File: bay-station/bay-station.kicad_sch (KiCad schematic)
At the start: 0 parts

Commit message: Add Power/BMS sheets: reverse-polarity protection, TVS, decoupling
Wristband power_bms.kicad_sch:
- JST-PH battery in -> AO3401A P-MOSFET reverse-polarity 'ideal diode'
  (source=batt+, gate pulled to GND via 100k) -> ESD5B5.0ST1G TVS across
  VBAT-GND -> DW01A+FS8205A single-cell protection (wired per Fortune
  Semiconductor's real datasheet application circuit) -> MCP73831 charger
  (USB-C power-only in, 6.8k PROG -> ~147mA, datasheet-exact CIN/COUT)
- NINA-B111/DWM3000 deliberately deferred to a future radio_mcu sheet
  (this sheet just produces a decoupled VBAT rail) -- see
  wristband/power_bms_notes.md
- ERC: 0 errors, 1 cosmetic warning (documented below)

Bay-station power_bms.kicad_sch:
- Barrel jack + USB-C power-only input (shared +5V_IN, each with reverse-
  polarity/TVS protection) alongside a backup Li-Ion input protected by
  its own AO3401A ideal-diode + TVS
- MCP73871 charge/power-path IC per Microchip's real typical application
  circuit (power-path/AC-DC-adapter mode, PROG1/PROG3 sized for 500mA
  fast-charge / 50mA termination, VPCC divider from the datasheet's own
  worked example) -> MAX17048 fuel gauge
- ESP32-S3-WROOM-1/DWM3000 anchors deferred to future connectivity/
  uwb_anchors sheets -- this sheet produces +VSYS (unregulated, tracks
  battery/input -- a dedicated 3.3V reg stage is a real open item) and
  VBATT_PROT
- ERC: 8 violations (1 error, 7 warnings), all single-member nets/pins
  reserved for hardware that doesn't exist until the connectivity sheet
  is built (e.g. MAX17048's SCL has no I2C host placed yet) -- see
  bay-station/power_bms_notes.md

Both sheets use global labels for net identity (no drawn wires), matching
the sibling wristband-alarm project's convention, and only reference
already-imported library parts plus KiCad-default generics (P-MOSFET,
TVS, R/C) -- no new custom symbols were needed on either board.

Notable gotcha found and documented: kicad-cli silently fails to load
(and silently treats as EMPTY, no error) a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
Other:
- added sheet Power BMS (power_bms.kicad_sch)
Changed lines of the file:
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@@
 		(comment 1 "UWB rescue locator -- bay station: 4x UWB anchor array + connectivity MCU + longevity-focused BMS")
+	)
+	(sheet
+		(at 30 30)
+		(size 60 40)
+		(fields_autoplaced yes)
+		(stroke
+			(width 0.1524)
+			(type solid)
+		)
+		(fill
+			(color 0 0 0 0.0000)
+		)
+		(property "Sheetname" "Power BMS"
+			(at 30 28.5 0)
+			(effects
+				(font
+					(size 1.27 1.27)
+				)
+				(justify left bottom)
+			)
+		)
+		(property "Sheetfile" "power_bms.kicad_sch"
+			(at 30 71.5 0)
+			(effects
+				(font
+					(size 1.27 1.27)
+				)
+				(justify left top)
+			)
+		)
+		(instances
+			(project "bay-station"
+				(path "/543ba435-6cf4-448c-821e-3c5778b02e9c"
+					(page "2")
+				)
+			)
+		)
 	)
 	(sheet_instances

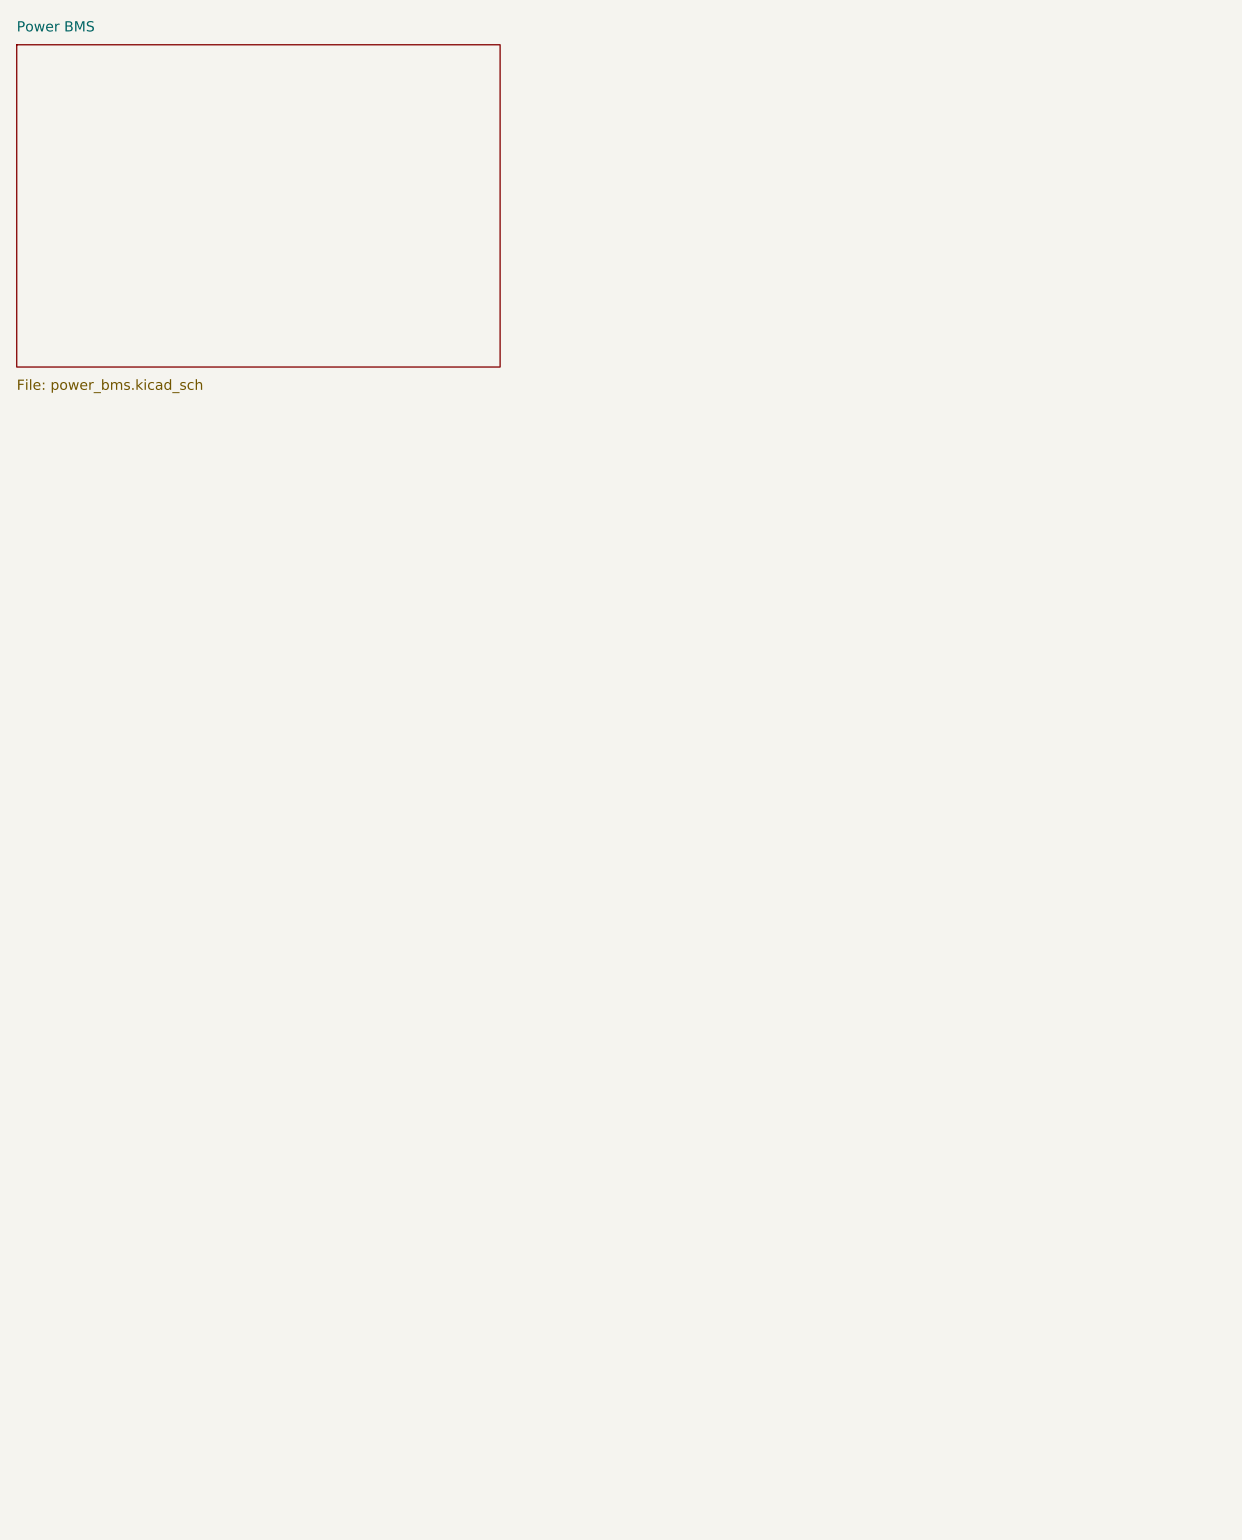
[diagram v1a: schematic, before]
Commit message: Add radio_mcu/mechanical (wristband) and connectivity/uwb_anchors/mechanical (bay-station) sheets
Placement-only pass, nothing wired (no wires, no global labels) -- per
request, this organizes the remaining confirmed components onto their
own hierarchical sheets rather than wiring them up yet:

Wristband:
- radio_mcu.kicad_sch: NINA-B111 (U3) + DWM3000 (U4), with 0603 decoupling
  caps placed near each supply pin (values are reasonable generic
  defaults, not yet confirmed against exact datasheet application-circuit
  numbers -- flagged in the sheet/README, revisit when wiring)
- mechanical.kicad_sch: 4x M2 mounting holes (H1-H4)

Bay-station:
- connectivity.kicad_sch: ESP32-S3-WROOM-1 (U3) + decoupling per
  Espressif's design guidelines (already cited in libs/README.md)
- uwb_anchors.kicad_sch: 4x DWM3000 anchor instances (U4-U7), each
  individually labeled and decoupled (values are typical-practice
  estimates, not independently re-verified against the datasheet's own
  application circuit -- flagged on the sheet itself)
- mechanical.kicad_sch: 4x mounting holes (H1-H4) + a note pointing at
  docs/decisions.md's open anchor-placement/enclosure item

Both boards: sheet hierarchy registered in the root .kicad_sch and the
project's sheets list, no reference-designator collisions with the
existing power_bms sheets. ERC shows the expected large jump in
'not connected'/'not driven' violations on the new sheets only (inherent
to placing components without wiring them) -- the existing power_bms
sheets' own violation counts are unchanged.

Also: bay-station's power_bms.kicad_sch/bay-station.kicad_sch/
bay-station.kicad_pro got silently reformatted to KiCad 10 file format by
a live KiCad GUI session that had the project open in the background
during this work (confirmed via reference-designator diff that no
component content was lost, just a version/format bump) -- wristband's
files are unaffected, still KiCad 8.0 format. Added bay-station's new
KiCad-10 '.history/' local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
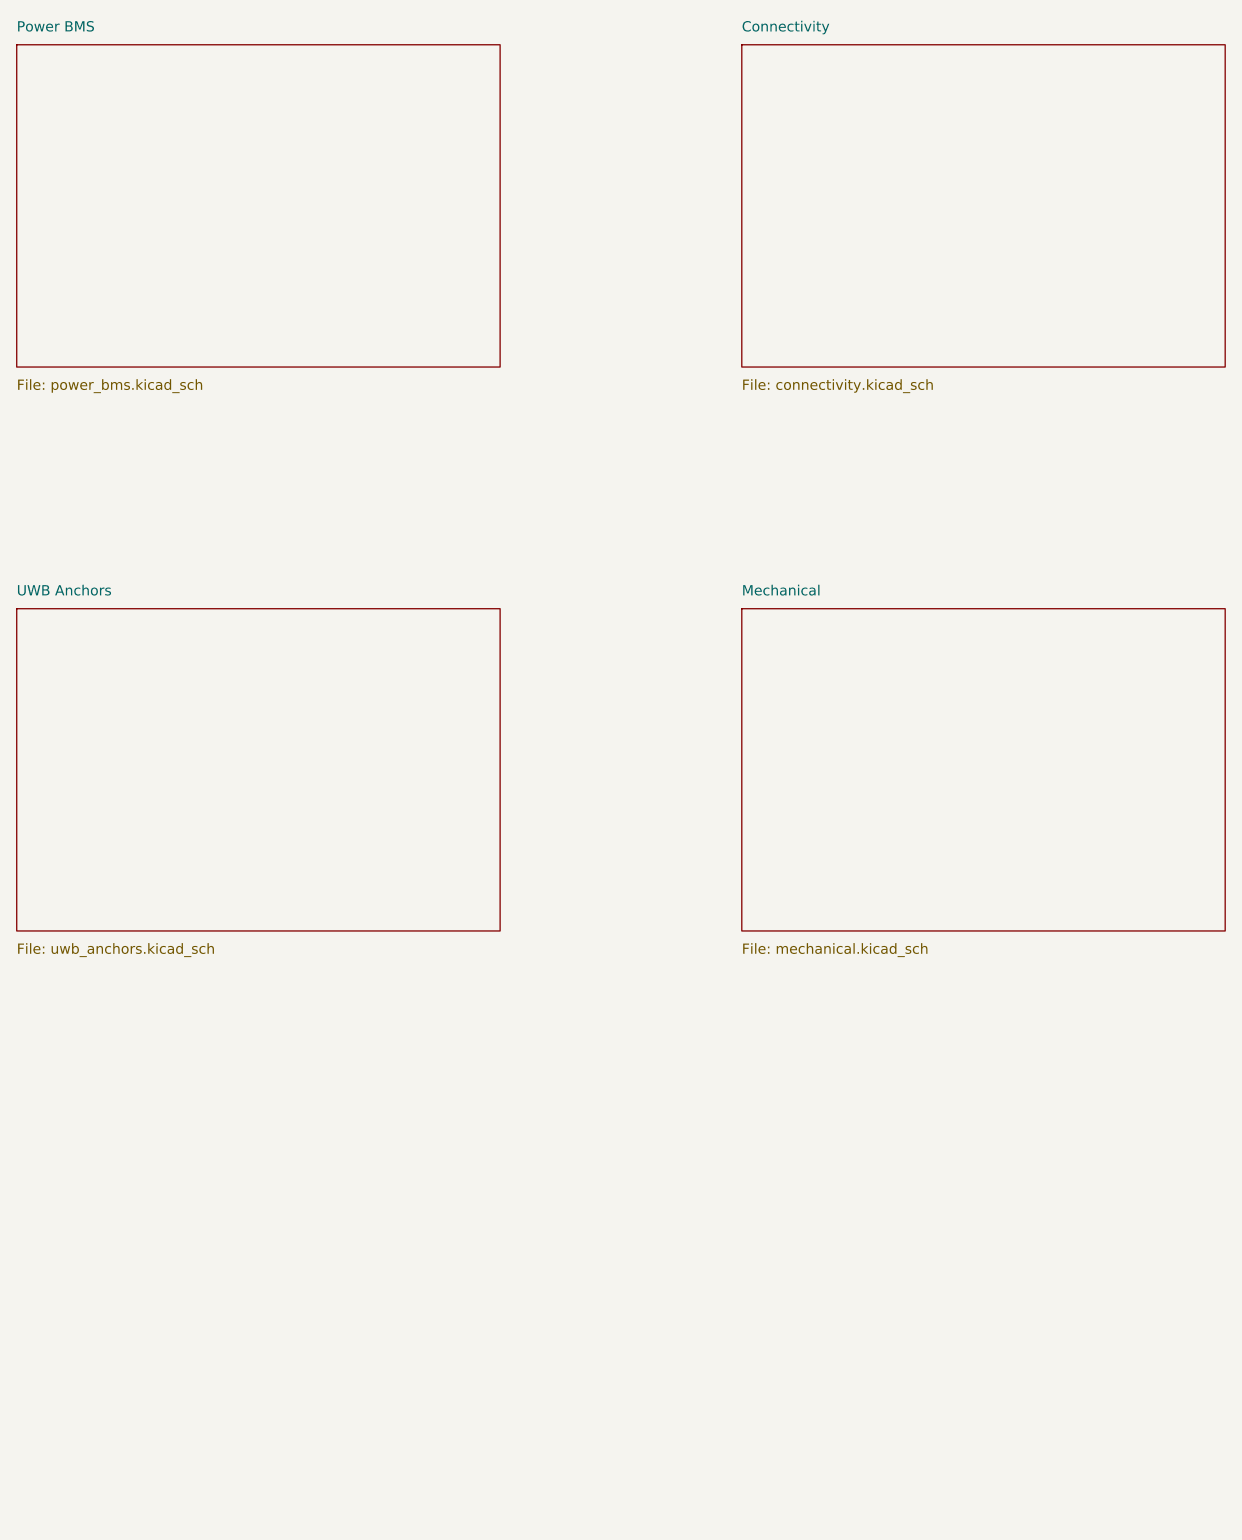
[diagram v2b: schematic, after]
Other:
- added sheet Connectivity (connectivity.kicad_sch)
- added sheet Mechanical (mechanical.kicad_sch)
- added sheet UWB Anchors (uwb_anchors.kicad_sch)
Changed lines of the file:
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@@
 (kicad_sch
-	(version 20231120)
+	(version 20260306)
 	(generator "eeschema")
-	(generator_version "8.0")
+	(generator_version "10.0")
 	(paper "A4")
 	(title_block
@@
 		(at 30 30)
 		(size 60 40)
+		(exclude_from_sim no)
+		(in_bom yes)
+		(on_board yes)
+		(dnp no)
 		(fields_autoplaced yes)
 		(stroke
@@
 		)
 		(fill
-			(color 0 0 0 0.0000)
+			(color 0 0 0 0)
 		)
 		(property "Sheetname" "Power BMS"
 			(at 30 28.5 0)
+			(show_name no)
+			(do_not_autoplace no)
 			(effects
 				(font
@@
 		(property "Sheetfile" "power_bms.kicad_sch"
 			(at 30 71.5 0)
+			(show_name no)
+			(do_not_autoplace no)
 			(effects
 				(font
@@
 		)
 	)
+	(sheet
+		(at 120 30)
+		(size 60 40)
+		(exclude_from_sim no)
+		(in_bom yes)
+		(on_board yes)
+		(dnp no)
+		(fields_autoplaced yes)
+		(stroke
+			(width 0.1524)
+			(type solid)
+		)
+		(fill
+			(color 0 0 0 0)
+		)
+		(property "Sheetname" "Connectivity"
+			(at 120 28.5 0)
+			(show_name no)
+			(do_not_autoplace no)
+			(effects
+				(font
+					(size 1.27 1.27)
+				)
+				(justify left bottom)
+			)
+		)
+		(property "Sheetfile" "connectivity.kicad_sch"
+			(at 120 71.5 0)
+			(show_name no)
+			(do_not_autoplace no)
+			(effects
+				(font
+					(size 1.27 1.27)
+				)
+				(justify left top)
+			)
+		)
+		(instances
+			(project "bay-station"
+				(path "/543ba435-6cf4-448c-821e-3c5778b02e9c"
+					(page "3")
+				)
+			)
+		)
+	)
+	(sheet
+		(at 30 100)
+		(size 60 40)
+		(exclude_from_sim no)
+		(in_bom yes)
+		(on_board yes)
+		(dnp no)
+		(fields_autoplaced yes)
+		(stroke
+			(width 0.1524)
+			(type solid)
+		)
+		(fill
+			(color 0 0 0 0)
+		)
+		(property "Sheetname" "UWB Anchors"
+			(at 30 98.5 0)
+			(show_name no)
+			(do_not_autoplace no)
+			(effects
+				(font
+					(size 1.27 1.27)
+				)
+				(justify left bottom)
+			)
+		)
+		(property "Sheetfile" "uwb_anchors.kicad_sch"
+			(at 30 141.5 0)
+			(show_name no)
+			(do_not_autoplace no)
+			(effects
+				(font
+					(size 1.27 1.27)
+				)
+				(justify left top)
+			)
+		)
+		(instances
+			(project "bay-station"
+				(path "/543ba435-6cf4-448c-821e-3c5778b02e9c"
+					(page "4")
+				)
+			)
+		)
+	)
+	(sheet
+		(at 120 100)
+		(size 60 40)
+		(exclude_from_sim no)
+		(in_bom yes)
+		(on_board yes)
+		(dnp no)
+		(fields_autoplaced yes)
+		(stroke
+			(width 0.1524)
+			(type solid)
+		)
+		(fill
+			(color 0 0 0 0)
+		)
+		(property "Sheetname" "Mechanical"
+			(at 120 98.5 0)
+			(show_name no)
+			(do_not_autoplace no)
+			(effects
+				(font
+					(size 1.27 1.27)
+				)
+				(justify left bottom)
+			)
+		)
+		(property "Sheetfile" "mechanical.kicad_sch"
+			(at 120 141.5 0)
+			(show_name no)
+			(do_not_autoplace no)
+			(effects
+				(font
+					(size 1.27 1.27)
+				)
+				(justify left top)
+			)
+		)
+		(instances
+			(project "bay-station"
+				(path "/543ba435-6cf4-448c-821e-3c5778b02e9c"
+					(page "5")
+				)
+			)
+		)
+	)
 	(sheet_instances
 		(path "/"
@@
 		)
 	)
+	(embedded_fonts no)
 )

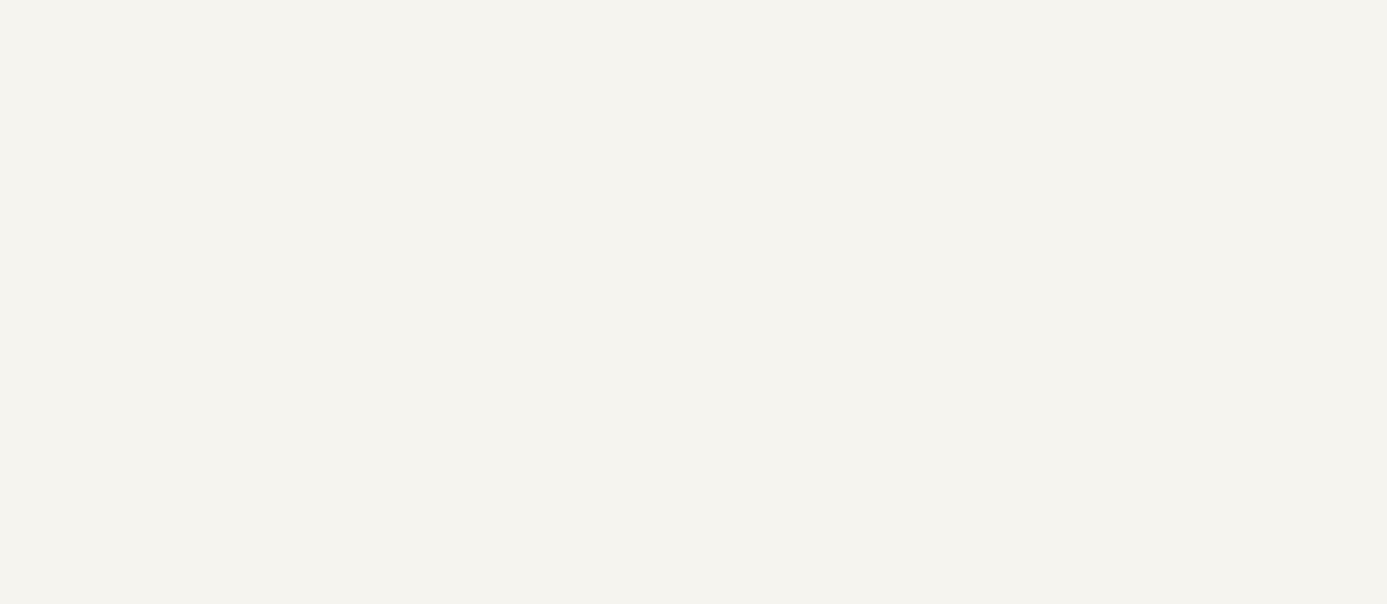
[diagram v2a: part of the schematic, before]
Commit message: Add regulation/antenna/programming-debug sheets; fix confirmed voltage-safety gap
Real datasheet check found a genuine hardware bug in progress, not just a
missing part: NINA-B111 abs-max VCC is 3.9V, DWM3000 abs-max VDD3V3 is
4.0V, but a fully-charged LiPo hits 4.2V -- both boards were about to feed
these ICs straight off the unregulated battery/system rail. Fixed via a
new dedicated regulation sheet per board (placement-only, not wired yet,
same as everything else at this stage):

- wristband/regulation.kicad_sch: MCP1700T-3302E/TT LDO (3.3V, low-Iq),
  current budget verified (NINA-B111 ~12mA + DWM3000 ~55mA vs 250mA
  rating, ~3.7x headroom)
- bay-station/regulation.kicad_sch: TPS62A02PDDCR buck converter (2A,
  single-cell-Li-Ion input range -- the very common TPS563201 was
  considered and rejected, its 4.5V input minimum is incompatible with a
  battery-only rail), current budget verified (ESP32-S3 ~355mA peak +
  4x DWM3000 ~55mA each vs 2A rating, ~3.5x headroom)

Also added, all confirmed against real datasheets:
- wristband/antenna.kicad_sch: ProAnt InSide-2400 BLE antenna (NINA-B111
  needs an external one per u-blox's approved-antenna list; DWM3000 has
  its own onboard antenna already, confirmed, no antenna sheet needed on
  the bay station)
- GPIO5/6 SPI-mode strapping pull-downs on every DWM3000 instance (both
  boards) -- required per Qorvo's own power-up timing diagrams
- wristband/programming_debug.kicad_sch: SWD header for NINA-B111
- bay-station/programming_debug.kicad_sch: ESP32-S3 boot-strap resistors,
  EN RC delay, BOOT/RESET buttons, native-USB flashing interface

One real inconsistency surfaced and flagged (not fixed) in
docs/decisions.md: the bay station's existing power-input USB-C has no
data pins, so a second, data-capable USB-C had to be added for ESP32-S3
flashing rather than consolidating into one connector -- needs a decision.

docs/decisions.md and README.md updated: new items marked resolved with
full reasoning, new open items ad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
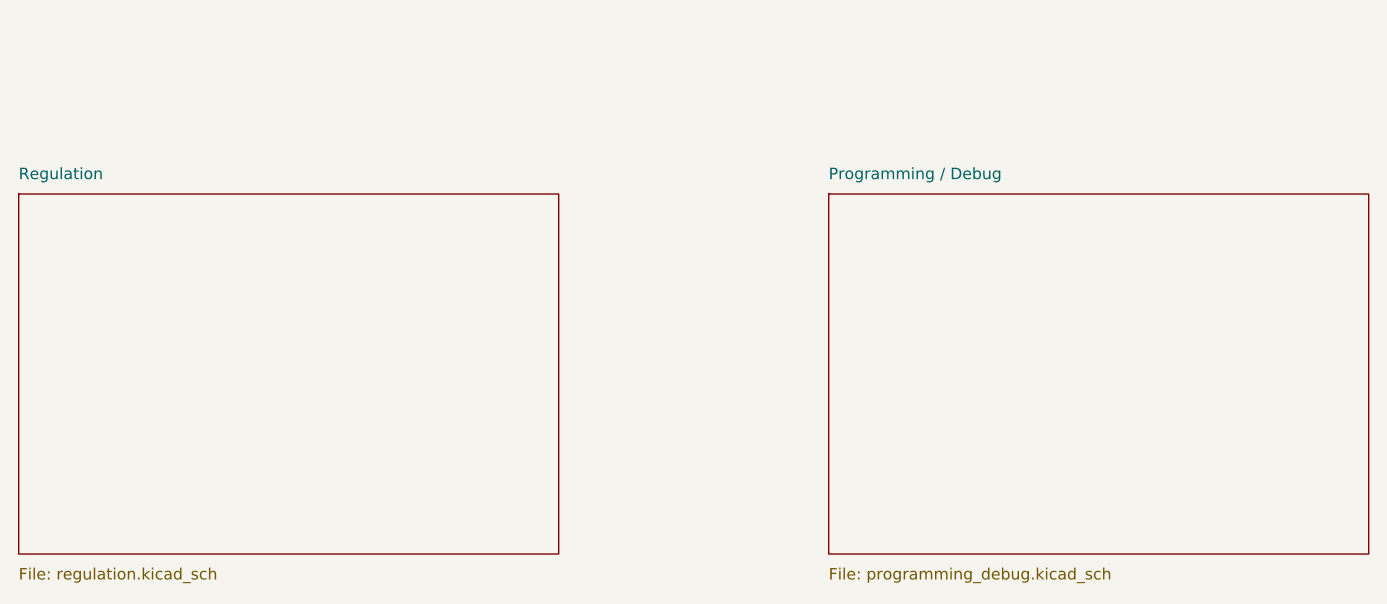
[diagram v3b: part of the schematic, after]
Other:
- added sheet Programming / Debug (programming_debug.kicad_sch)
- added sheet Regulation (regulation.kicad_sch)
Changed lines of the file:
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@@
+		)
+	)
+	(sheet
+		(at 30 170)
+		(size 60 40)
+		(exclude_from_sim no)
+		(in_bom yes)
+		(on_board yes)
+		(dnp no)
+		(fields_autoplaced yes)
+		(stroke
+			(width 0.1524)
+			(type solid)
+		)
+		(fill
+			(color 0 0 0 0)
+		)
+		(property "Sheetname" "Regulation"
+			(at 30 168.5 0)
+			(show_name no)
+			(do_not_autoplace no)
+			(effects
+				(font
+					(size 1.27 1.27)
+				)
+				(justify left bottom)
+			)
+		)
+		(property "Sheetfile" "regulation.kicad_sch"
+			(at 30 211.5 0)
+			(show_name no)
+			(do_not_autoplace no)
+			(effects
+				(font
+					(size 1.27 1.27)
+				)
+				(justify left top)
+			)
+		)
+		(instances
+			(project "bay-station"
+				(path "/543ba435-6cf4-448c-821e-3c5778b02e9c"
+					(page "6")
+				)
+			)
+		)
+	)
+	(sheet
+		(at 120 170)
+		(size 60 40)
+		(exclude_from_sim no)
+		(in_bom yes)
+		(on_board yes)
+		(dnp no)
+		(fields_autoplaced yes)
+		(stroke
+			(width 0.1524)
+			(type solid)
+		)
+		(fill
+			(color 0 0 0 0)
+		)
+		(property "Sheetname" "Programming / Debug"
+			(at 120 168.5 0)
+			(show_name no)
+			(do_not_autoplace no)
+			(effects
+				(font
+					(size 1.27 1.27)
+				)
+				(justify left bottom)
+			)
+		)
+		(property "Sheetfile" "programming_debug.kicad_sch"
+			(at 120 211.5 0)
+			(show_name no)
+			(do_not_autoplace no)
+			(effects
+				(font
+					(size 1.27 1.27)
+				)
+				(justify left top)
+			)
+		)
+		(instances
+			(project "bay-station"
+				(path "/543ba435-6cf4-448c-821e-3c5778b02e9c"
+					(page "7")
+				)
+			)
 		)
 	)
